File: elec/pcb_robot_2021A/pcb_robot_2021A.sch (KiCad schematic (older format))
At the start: 18 parts

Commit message: Connectique lidar hokuyo
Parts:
- added J?: Conn_bat_power, symbol Connector:Screw_Terminal_01x02
- added U?: mosfet_lid_I2, mosfets:SOT-23, symbol mySymbols:IRLML6344
- added U?: mosfet_lid_I1, mosfets:SOT-23, symbol mySymbols:IRLML6344
- added U?: mosfet_lid_I4, mosfets:SOT-23, symbol mySymbols:IRLML6344
- added U?: mosfet_lid_I5, mosfets:SOT-23, symbol mySymbols:IRLML6344
- added U?: mosfet_lid_I3, mosfets:SOT-23, symbol mySymbols:IRLML6344
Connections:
- net labels added: Xbee_RX, Xbee_TX, lidard_in1, lidard_in2, lidard_in3, lidard_in4, lidard_in5
- wire segments 59 -> 86
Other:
- moved on the sheet: C?, J?, U?

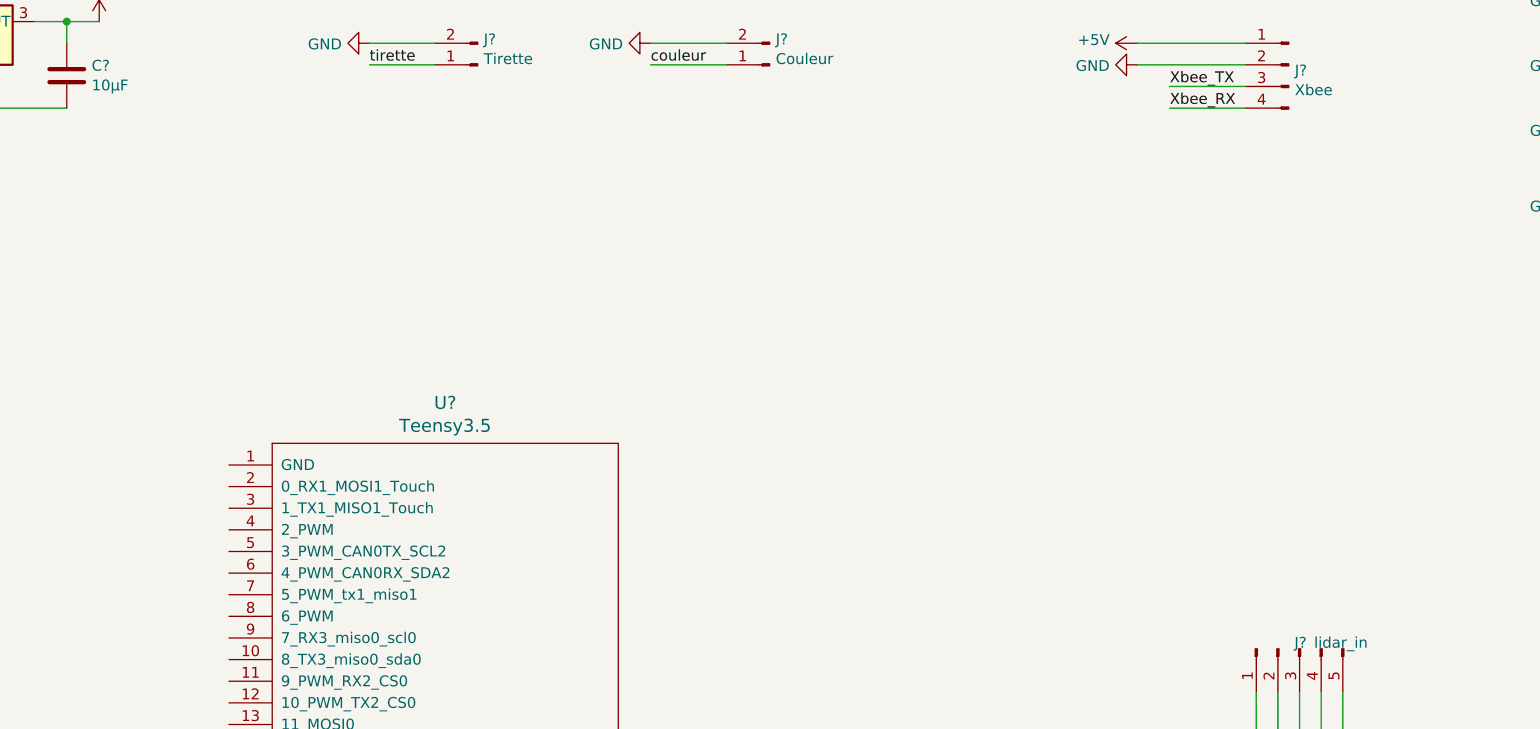
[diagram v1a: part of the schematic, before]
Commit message: add PCA9685 conn on main card
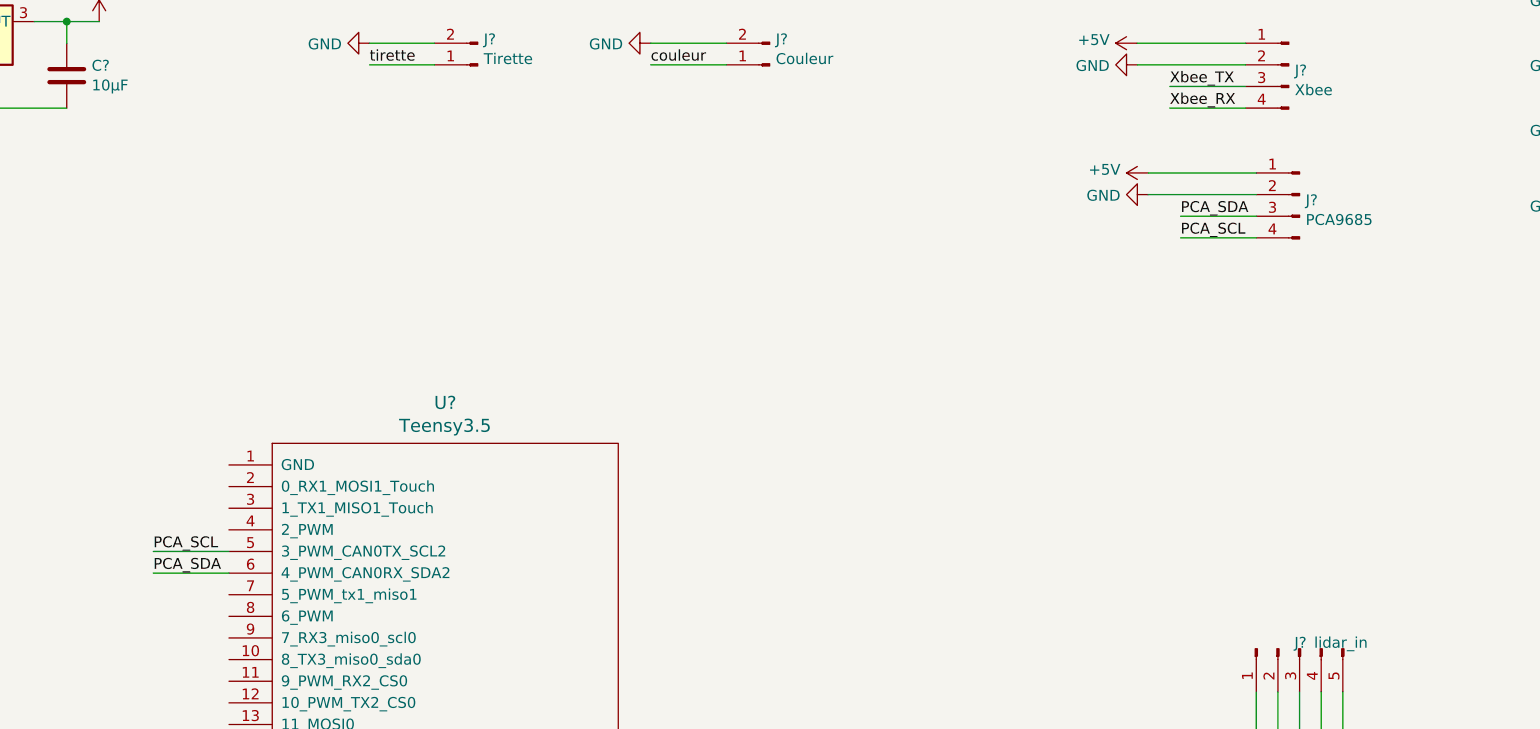
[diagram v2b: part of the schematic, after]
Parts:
- added J?: PCA9685, symbol Connector:Conn_01x04_Male
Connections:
- net +5V: now also J?.1 (Pin_1)
- net GND: now also J?.2 (Pin_2)
- net PCA_SCL: now reaches U?.5 (3_PWM_CAN0TX_SCL2)
- net PCA_SCL: now also J?.4 (Pin_4)
- net PCA_SDA: now reaches U?.6 (4_PWM_CAN0RX_SDA2)
- net PCA_SDA: now also J?.3 (Pin_3)
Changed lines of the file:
@@
 Wire Wire Line
 	5550 7050 5950 7050
+$Comp
+L Connector:Conn_01x04_Male J?
+U 1 1 60565B56
+P 8500 1600
+F 0 "J?" H 8472 1574 50  0000 R CNN
+F 1 "PCA9685" H 8472 1483 50  0000 R CNN
+F 2 "" H 8500 1600 50  0001 C CNN
+F 3 "~" H 8500 1600 50  0001 C CNN
+	1    8500 1600
+	-1   0    0    -1
+$EndComp
+$Comp
+L power:+5V #PWR?
+U 1 1 60565B5C
+P 7800 1500
+F 0 "#PWR?" H 7800 1350 50  0001 C CNN
+F 1 "+5V" V 7815 1628 50  0000 L CNN
+F 2 "" H 7800 1500 50  0001 C CNN
+F 3 "" H 7800 1500 50  0001 C CNN
+	1    7800 1500
+	0    -1   -1   0
+$EndComp
+$Comp
+L power:GND #PWR?
+U 1 1 60565B62
+P 7800 1600
+F 0 "#PWR?" H 7800 1350 50  0001 C CNN
+F 1 "GND" V 7805 1472 50  0000 R CNN
+F 2 "" H 7800 1600 50  0001 C CNN
+F 3 "" H 7800 1600 50  0001 C CNN
+	1    7800 1600
+	0    1    1    0
+$EndComp
+Wire Wire Line
+	7800 1500 8300 1500
+Wire Wire Line
+	8300 1600 7800 1600
+Text Label 7950 1700 0    50   ~ 0
+PCA_SDA
+Text Label 7950 1800 0    50   ~ 0
+PCA_SCL
+Wire Wire Line
+	7950 1700 8300 1700
+Wire Wire Line
+	8300 1800 7950 1800
+Text Label 3200 3350 0    50   ~ 0
+PCA_SDA
+Text Label 3200 3250 0    50   ~ 0
+PCA_SCL
+Wire Wire Line
+	3200 3350 3550 3350
+Wire Wire Line
+	3550 3250 3200 3250
 $EndSCHEMATC

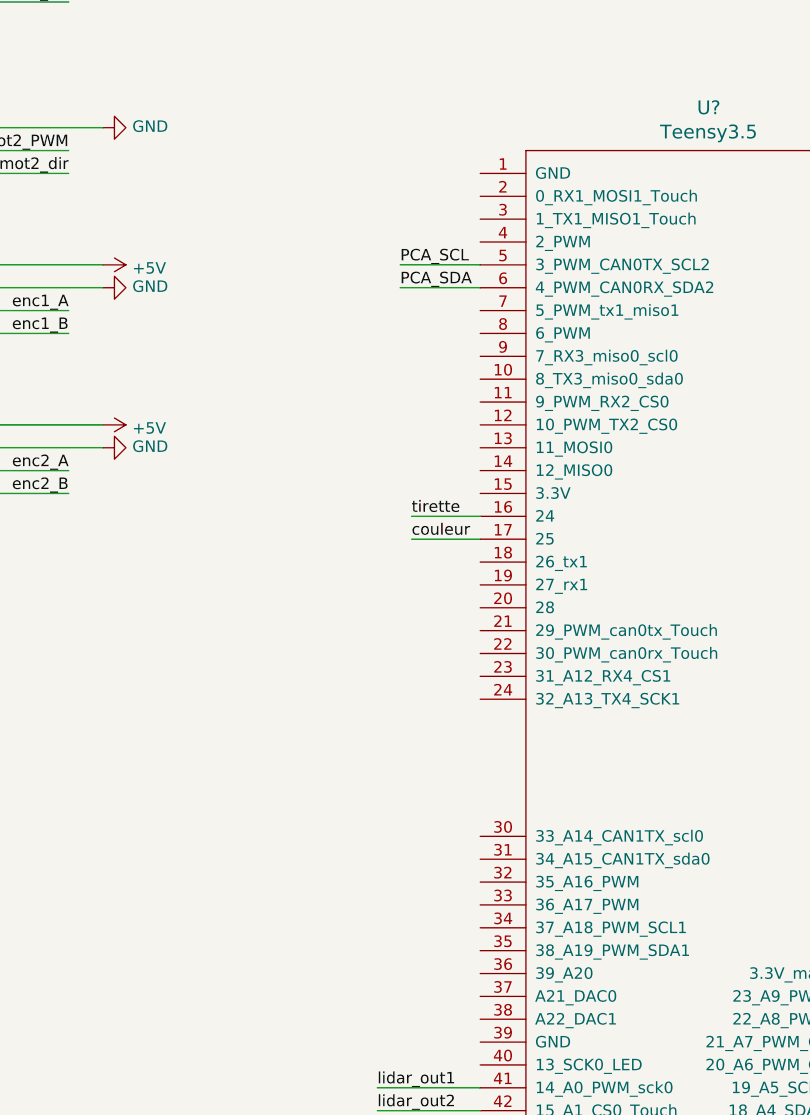
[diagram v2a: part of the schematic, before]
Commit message: update conn on teensy
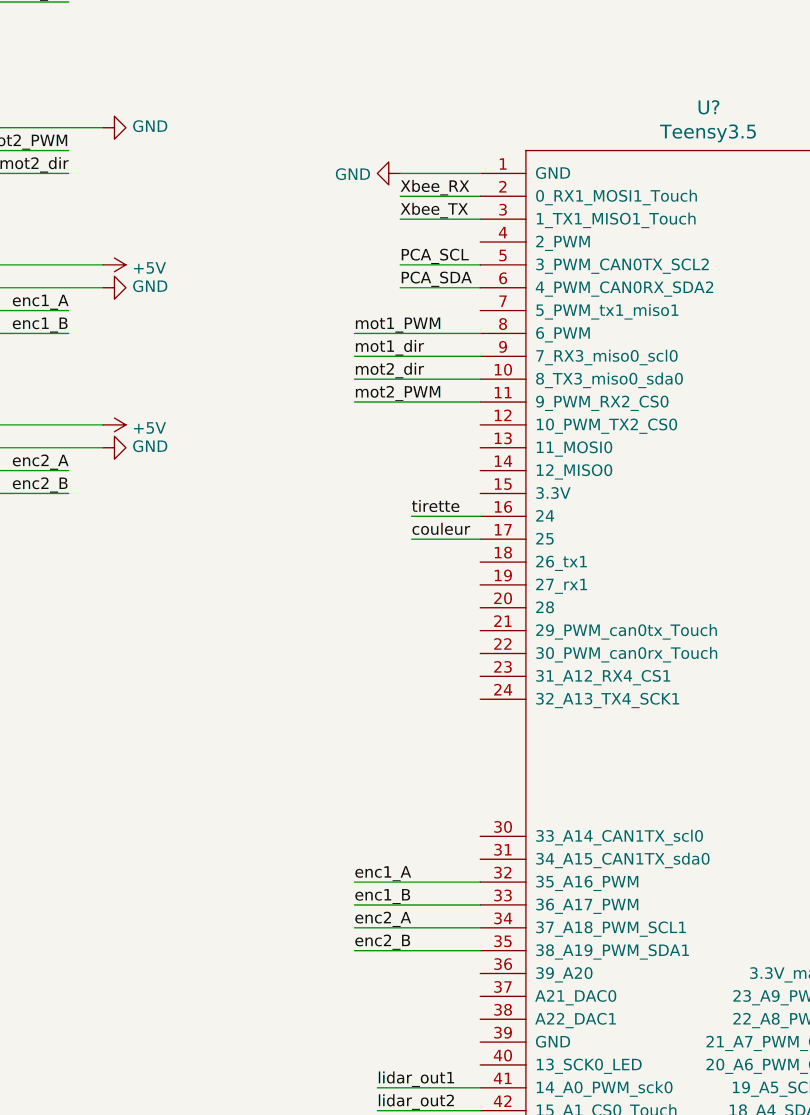
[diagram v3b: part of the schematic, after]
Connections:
- net GND: now also U?.1 (GND)
- net Xbee_RX: now also U?.2 (0_RX1_MOSI1_Touch)
- net Xbee_TX: now also U?.3 (1_TX1_MISO1_Touch)
- net enc1_A: now also U?.32 (35_A16_PWM)
- net enc1_B: now also U?.33 (36_A17_PWM)
- net enc2_A: now also U?.34 (37_A18_PWM_SCL1)
- net enc2_B: now also U?.35 (38_A19_PWM_SDA1)
- net mot1_PWM: now also U?.8 (6_PWM)
- net mot1_dir: now also U?.9 (7_RX3_miso0_scl0)
- net mot2_PWM: now also U?.11 (9_PWM_RX2_CS0)
- net mot2_dir: now also U?.10 (8_TX3_miso0_sda0)
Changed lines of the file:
@@
 Title "Carte principale Robot 2021 A"
 Date "2021-02-21"
-Rev "v0.2"
+Rev "v0.3"
 Comp "ENAC Robotique"
-Comment1 "Connectique du lidar Hokuyo"
+Comment1 ""
 Comment2 ""
 Comment3 ""
@@
 Wire Wire Line
 	3550 3250 3200 3250
+Text Label 3200 3050 0    50   ~ 0
+Xbee_TX
+Text Label 3200 2950 0    50   ~ 0
+Xbee_RX
+Wire Wire Line
+	3200 3050 3550 3050
+Wire Wire Line
+	3550 2950 3200 2950
+Text Label 3000 6150 0    50   ~ 0
+enc2_A
+Text Label 3000 6250 0    50   ~ 0
+enc2_B
+Wire Wire Line
+	3550 6150 3000 6150
+Wire Wire Line
+	3000 6250 3550 6250
+Text Label 3000 5950 0    50   ~ 0
+enc1_A
+Text Label 3000 6050 0    50   ~ 0
+enc1_B
+Wire Wire Line
+	3550 5950 3000 5950
+Wire Wire Line
+	3000 6050 3550 6050
+Text Label 3000 3850 0    50   ~ 0
+mot2_PWM
+Text Label 3000 3750 0    50   ~ 0
+mot2_dir
+Wire Wire Line
+	3550 3850 3000 3850
+Wire Wire Line
+	3550 3750 3000 3750
+Text Label 3000 3550 0    50   ~ 0
+mot1_PWM
+Text Label 3000 3650 0    50   ~ 0
+mot1_dir
+Wire Wire Line
+	3550 3550 3000 3550
+Wire Wire Line
+	3550 3650 3000 3650
+$Comp
+L power:GND #PWR?
+U 1 1 605E2831
+P 3200 2850
+F 0 "#PWR?" H 3200 2600 50  0001 C CNN
+F 1 "GND" V 3205 2722 50  0000 R CNN
+F 2 "" H 3200 2850 50  0001 C CNN
+F 3 "" H 3200 2850 50  0001 C CNN
+	1    3200 2850
+	0    1    1    0
+$EndComp
+Wire Wire Line
+	3200 2850 3550 2850
 $EndSCHEMATC

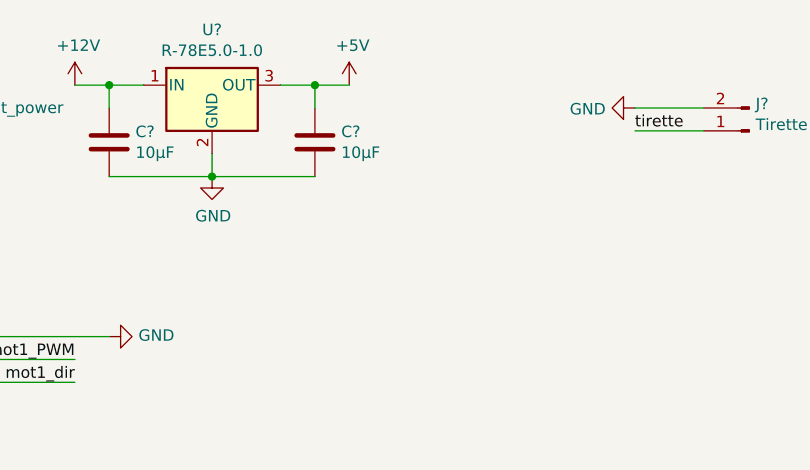
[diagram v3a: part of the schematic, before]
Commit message: schematic for PCA9685 (conn 8 servos)
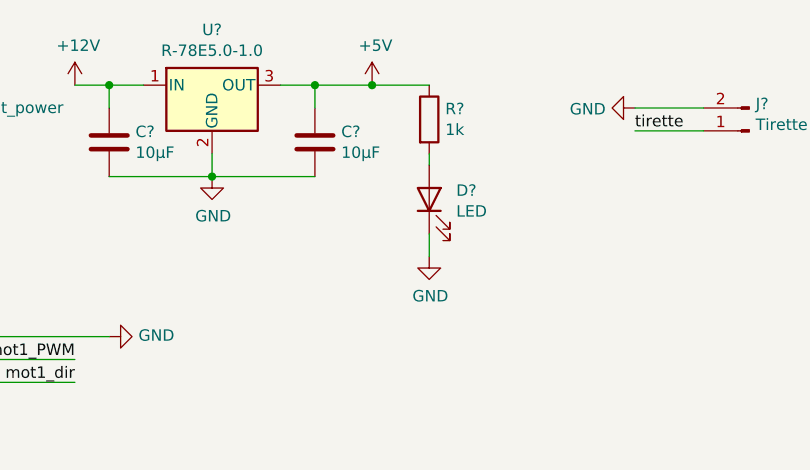
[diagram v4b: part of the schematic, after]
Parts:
- added D?: LED, symbol Device:LED
- added R?: 1k, symbol Device:R
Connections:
- net +5V: now also R?.1
- net GND: now also D?.1 (K)
- new net: D?.2 (A), R?.2
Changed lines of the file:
@@
 L power:+5V #PWR?
 U 1 1 60326623
-P 2950 800
-F 0 "#PWR?" H 2950 650 50  0001 C CNN
-F 1 "+5V" H 2965 973 50  0000 C CNN
-F 2 "" H 2950 800 50  0001 C CNN
-F 3 "" H 2950 800 50  0001 C CNN
-	1    2950 800
+P 3050 800
+F 0 "#PWR?" H 3050 650 50  0001 C CNN
+F 1 "+5V" H 3065 973 50  0000 C CNN
+F 2 "" H 3050 800 50  0001 C CNN
+F 3 "" H 3050 800 50  0001 C CNN
+	1    3050 800
 	1    0    0    -1
 $EndComp
@@
 $EndComp
 Wire Wire Line
-	2950 800  2800 800
-Wire Wire Line
 	2800 1200 2350 1200
 Connection ~ 2350 1200
@@
 Wire Wire Line
 	2800 900  2800 800
-Connection ~ 2800 800
 Wire Wire Line
 	2800 800  2650 800
@@
 Wire Wire Line
 	3200 2850 3550 2850
+$Comp
+L Device:R R?
+U 1 1 606656D7
+P 3300 950
+F 0 "R?" H 3370 996 50  0000 L CNN
+F 1 "1k" H 3370 905 50  0000 L CNN
+F 2 "" V 3230 950 50  0001 C CNN
+F 3 "~" H 3300 950 50  0001 C CNN
+	1    3300 950
+	1    0    0    -1
+$EndComp
+Wire Wire Line
+	2800 800  3050 800
+Connection ~ 2800 800
+Wire Wire Line
+	3050 800  3300 800
+Connection ~ 3050 800
+$Comp
+L Device:LED D?
+U 1 1 60675F57
+P 3300 1300
+F 0 "D?" V 3339 1182 50  0000 R CNN
+F 1 "LED" V 3248 1182 50  0000 R CNN
+F 2 "" H 3300 1300 50  0001 C CNN
+F 3 "~" H 3300 1300 50  0001 C CNN
+	1    3300 1300
+	0    -1   -1   0
+$EndComp
+$Comp
+L power:GND #PWR?
+U 1 1 60676A3D
+P 3300 1550
+F 0 "#PWR?" H 3300 1300 50  0001 C CNN
+F 1 "GND" H 3305 1377 50  0000 C CNN
+F 2 "" H 3300 1550 50  0001 C CNN
+F 3 "" H 3300 1550 50  0001 C CNN
+	1    3300 1550
+	1    0    0    -1
+$EndComp
+Wire Wire Line
+	3300 1100 3300 1150
+Wire Wire Line
+	3300 1450 3300 1550
 $EndSCHEMATC

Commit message: fin v1 PCA et main carte
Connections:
- no-connect marks 0 -> 15
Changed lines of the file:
@@
 Wire Wire Line
 	3300 1450 3300 1550
+NoConn ~ 5550 6250
+NoConn ~ 5550 6350
+NoConn ~ 5550 6450
+NoConn ~ 5550 6550
+NoConn ~ 3550 6750
+NoConn ~ 3550 6650
+NoConn ~ 3550 6550
+NoConn ~ 3550 6450
+NoConn ~ 3550 6350
+NoConn ~ 3550 3150
+NoConn ~ 3550 3450
+NoConn ~ 3550 3950
+NoConn ~ 3550 4250
+NoConn ~ 3550 4150
+NoConn ~ 3550 4050
 $EndSCHEMATC

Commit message: fin sch carte principale
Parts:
- added J1: LCD, Connector_JST:JST_XH_B4B-XH-A_1x04_P2.50mm_Vertical, symbol Connector:Conn_01x04_Male
- added J15: UART_backup, Connector_JST:JST_XH_B4B-XH-A_1x04_P2.50mm_Vertical, symbol Connector:Conn_01x04_Male
- added J18: Capt_US, Connector_JST:JST_XH_B4B-XH-A_1x04_P2.50mm_Vertical, symbol Connector:Conn_01x04_Male
- added J19: I2C_backup, Connector_JST:JST_XH_B4B-XH-A_1x04_P2.50mm_Vertical, symbol Connector:Conn_01x04_Male
- added J2: IR 1.1, Connector_JST:JST_XH_B3B-XH-A_1x03_P2.50mm_Vertical, symbol Connector:Conn_01x03_Male
- added J3: IR 1.2, Connector_JST:JST_XH_B3B-XH-A_1x03_P2.50mm_Vertical, symbol Connector:Conn_01x03_Male
- added J4: IR 1.3, Connector_JST:JST_XH_B3B-XH-A_1x03_P2.50mm_Vertical, symbol Connector:Conn_01x03_Male
- added J5: IR 2.1, Connector_JST:JST_XH_B3B-XH-A_1x03_P2.50mm_Vertical, symbol Connector:Conn_01x03_Male
- added J6: IR 2.2, Connector_JST:JST_XH_B3B-XH-A_1x03_P2.50mm_Vertical, symbol Connector:Conn_01x03_Male
- added J7: IR 2.3, Connector_JST:JST_XH_B3B-XH-A_1x03_P2.50mm_Vertical, symbol Connector:Conn_01x03_Male
- added R1, R2: 2.2k, Resistor_SMD:R_0805_2012Metric_Pad1.15x1.40mm_HandSolder, symbol Device:R
- C1, C2: renamed from C?; footprint (none) -> Capacitor_SMD:C_0805_2012Metric_Pad1.15x1.40mm_HandSolder
- D1: renamed from D?; value LED -> LED_bleue; footprint (none) -> LED_SMD:LED_0603_1608Metric_Pad1.05x0.95mm_HandSolder
- J10, J11, J16, J17, J22: renamed from J?; footprint (none) -> Connector_JST:JST_XH_B4B-XH-A_1x04_P2.50mm_Vertical
- J12: renamed from J?; footprint (none) -> TerminalBlock:TerminalBlock_bornier-2_P5.08mm
- J13, J14, J23, J24, J25, J26: renamed from J?; footprint (none) -> Connector_JST:JST_XH_B2B-XH-A_1x02_P2.50mm_Vertical
- J20: renamed from J?; footprint (none) -> Connector_PinHeader_2.54mm:PinHeader_1x05_P2.54mm_Vertical
- J21: renamed from J?; footprint (none) -> Connector_PinHeader_2.54mm:PinHeader_1x03_P2.54mm_Vertical
- J8, J9: renamed from J?; footprint (none) -> Connector_JST:JST_XH_B3B-XH-A_1x03_P2.50mm_Vertical
- R3: renamed from R?; footprint (none) -> Resistor_SMD:R_0805_2012Metric_Pad1.15x1.40mm_HandSolder
- U2: renamed from U?; footprint (none) -> myFootprints:Teensy35_36
- U3, U4, U5, U6, U7: renamed from U?; footprint mosfets:SOT-23 -> myFootprints:SOT-23
- gave numbers to parts that had none: 1
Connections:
- net lidard_in1 is gone; now on net lidar_in1: U3.1 (G)
- net lidard_in2 is gone; now on net lidar_in2: U4.1 (G)
- net lidard_in3 is gone; now on net lidar_in3: U5.1 (G)
- net lidard_in4 is gone; now on net lidar_in4: U6.1 (G)
- net lidard_in5 is gone; now on net lidar_in5: U7.1 (G)
- net +5V: now also J1.1 (Pin_1), J15.1 (Pin_1), J18.1 (Pin_1), J19.1 (Pin_1), J2.1 (Pin_1), J3.1 (Pin_1), J4.1 (Pin_1), J5.1 (Pin_1), J6.1 (Pin_1), J7.1 (Pin_1), R1.1, R2.2
- net GND: now also J1.2 (Pin_2), J15.2 (Pin_2), J18.2 (Pin_2), J19.2 (Pin_2), J2.2 (Pin_2), J3.2 (Pin_2), J4.2 (Pin_2), J5.2 (Pin_2), J6.2 (Pin_2), J7.2 (Pin_2)
- net couleur: now also U2.7 (5_PWM_tx1_miso1); no longer U2.17 (25)
- net enc1_A: now also U2.43 (16_A2_scl0_Touch); no longer U2.32 (35_A16_PWM)
- net enc1_B: now also U2.44 (17_A3_sda0_Touch); no longer U2.33 (36_A17_PWM)
- net enc2_A: now also U2.21 (29_PWM_can0tx_Touch); no longer U2.34 (37_A18_PWM_SCL1)
- net enc2_B: now also U2.22 (30_PWM_can0rx_Touch); no longer U2.35 (38_A19_PWM_SDA1)
- net galet_1.1: now also U2.13 (11_MOSI0)
- net galet_1.2: now also U2.14 (12_MISO0)
- net galet_2.1: now also U2.41 (14_A0_PWM_sck0)
- net galet_2.2: now also U2.42 (15_A1_CS0_Touch)
- net lidar_in1: now also U2.49 (22_A8_PWM_Touch); no longer U2.48 (21_A7_PWM_CS0_sck1)
- net lidar_in2: now also U2.48 (21_A7_PWM_CS0_sck1); no longer U2.47 (20_A6_PWM_CS0_sck1)
- net lidar_in3: now also U2.47 (20_A6_PWM_CS0_sck1); no longer U2.46 (19_A5_SCL0_Touch)
- net lidar_in4: now also U2.46 (19_A5_SCL0_Touch); no longer U2.45 (18_A4_SDA0_Touch)
- net lidar_in5: now also U2.45 (18_A4_SDA0_Touch); no longer U2.44 (17_A3_sda0_Touch)
- net lidar_out1: now also U2.16 (24); no longer U2.41 (14_A0_PWM_sck0)
- net lidar_out2: now also U2.17 (25); no longer U2.42 (15_A1_CS0_Touch)
- net lidar_out3: now also U2.18 (26_tx1); no longer U2.43 (16_A2_scl0_Touch)
- net tirette: now also U2.12 (10_PWM_TX2_CS0); no longer U2.16 (24)
- net LCD_1: now reaches U2.19 (27_rx1)
- net LCD_1: now also J1.3 (Pin_3)
- net LCD_2: now reaches U2.20 (28)
- net LCD_2: now also J1.4 (Pin_4)
- net RX4: now reaches U2.23 (31_A12_RX4_CS1)
- net RX4: now also J15.4 (Pin_4)
- net TX4: now reaches U2.24 (32_A13_TX4_SCK1)
- net TX4: now also J15.3 (Pin_3)
- net IR_out1.1: now reaches U2.30 (33_A14_CAN1TX_scl0)
- net IR_out1.1: now also J2.3 (Pin_3)
- net IR_out1.2: now reaches U2.31 (34_A15_CAN1TX_sda0)
- net IR_out1.2: now also J3.3 (Pin_3)
- net PCA_SCL renamed SCL
- net SCL: now also J18.4 (Pin_4), J19.4 (Pin_4), R1.2
- net PCA_SDA renamed SDA
- net SDA: now also J18.3 (Pin_3), J19.3 (Pin_3), R2.1
- new net IR_out1.3: J4.3 (Pin_3), U2.32 (35_A16_PWM)
- new net IR_out2.1: J5.3 (Pin_3), U2.33 (36_A17_PWM)
- new net IR_out2.2: J6.3 (Pin_3), U2.34 (37_A18_PWM_SCL1)
- new net IR_out2.3: J7.3 (Pin_3), U2.35 (38_A19_PWM_SDA1)
- no-connect marks 15 -> 10
